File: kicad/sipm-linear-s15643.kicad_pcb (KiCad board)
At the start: 4 copper layers, 113.2 x 74.6 mm, 220 parts, among them J1 SSQ-103-01-G-D, J10 Conn_Coaxial, J11 Conn_Coaxial, J12 Conn_Coaxial, J13 Conn_Coaxial, J14 Conn_Coaxial, J15 Conn_Coaxial, J16 Conn_Coaxial, J17 Conn_Coaxial, J2 Conn_Coaxial, J3 Conn_Coaxial, J4 Conn_Coaxial, J5 Conn_Coaxial, J6 Conn_Coaxial, J7 Conn_Coaxial, J8 Conn_Coaxial, J9 Conn_Coaxial, U1 OPA847IDBVT, U10 OPA847IDBVT, U11 OPA847IDBVT, U12 OPA847IDBVT, U13 OPA847IDBVT, U14 OPA847IDBVT, U15 OPA847IDBVT, U16 OPA847IDBVT, U17 OPA847IDBVT, U2 S15643, U3 OPA847IDBVT, U4 OPA847IDBVT, U5 OPA847IDBVT, U6 OPA847IDBVT, U7 OPA847IDBVT, U8 OPA847IDBVT, U9 OPA847IDBVT

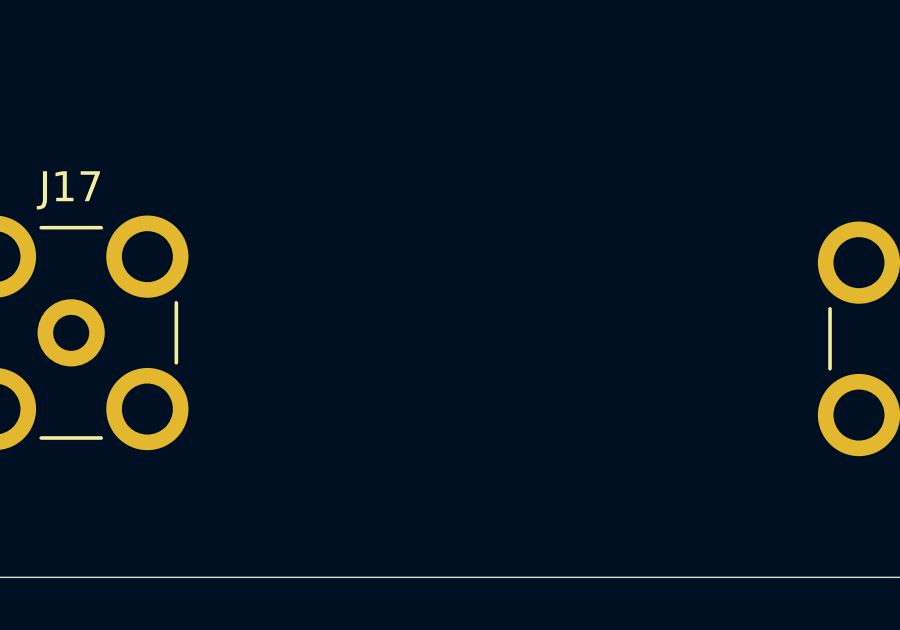
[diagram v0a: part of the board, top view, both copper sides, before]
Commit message: Split power rails across two power supplies
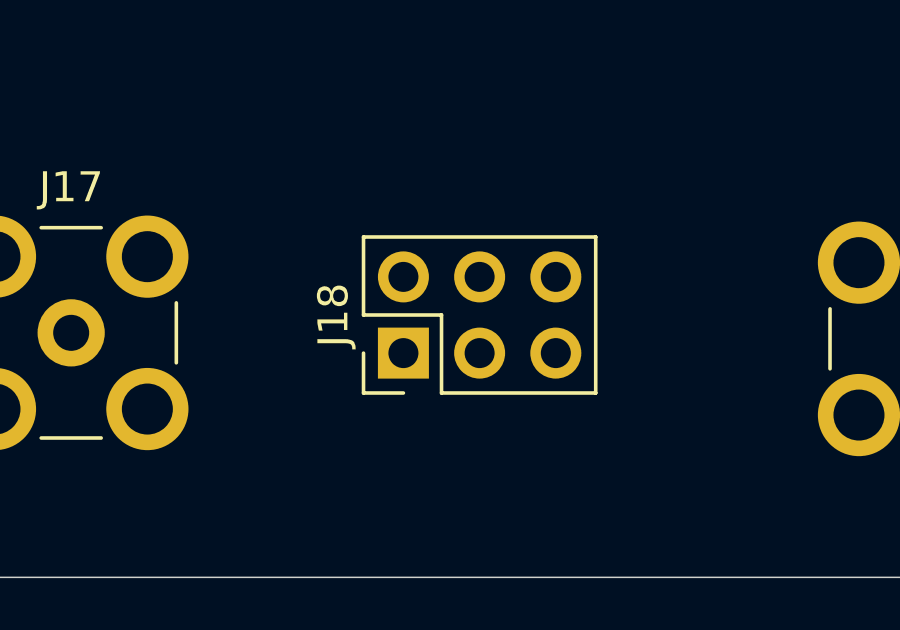
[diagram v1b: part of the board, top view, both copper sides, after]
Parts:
- added J18: SSQ-103-01-G-D, footprints:PinHeader_2x03_P2.54mm_Vertical, F.Cu at (182.7, 135.9)
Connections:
- C31 pad 1: VDDA -> /VSSA2
- C32 pad 1: VSSA -> /VDDA2
- C33 pad 1: VDDA -> /VSSA2
- C34 pad 1: VSSA -> /VDDA2
- C57 pad 1: VDDA -> /VSSA2
- C58 pad 1: VSSA -> /VDDA2
- C59 pad 1: VDDA -> /VSSA2
- C60 pad 1: VSSA -> /VDDA2
- C65 pad 1: VDDA -> /VSSA2
- C66 pad 1: VSSA -> /VDDA2
- C67 pad 1: VDDA -> /VSSA2
- C68 pad 1: VSSA -> /VDDA2
- C73 pad 1: VDDA -> /VSSA2
- C74 pad 1: VSSA -> /VDDA2
- C75 pad 1: VDDA -> /VSSA2
- C76 pad 1: VSSA -> /VDDA2
- J1 pad 1: (no net) -> +5V
- R105 pad 1: /SipmPair7/LINE -> LINE
- R106 pad 2: /SipmPair7/LINE -> LINE
- R14 pad 1: /SipmPair/LINE -> LINE
- R15 pad 2: /SipmPair/LINE -> LINE
- R25 pad 1: /SipmPair2/LINE -> LINE
- R26 pad 2: /SipmPair2/LINE -> LINE
- R37 pad 1: /SipmPair3/LINE -> LINE
- R38 pad 2: /SipmPair3/LINE -> LINE
- R49 pad 1: /SipmPair4/LINE -> LINE
- R50 pad 2: /SipmPair4/LINE -> LINE
- R59 pad 1: (no net) -> /VBias2
- R6 pad 1: /SipmPair1/LINE -> LINE
- R7 pad 2: /SipmPair1/LINE -> LINE
- R81 pad 1: /SipmPair5/LINE -> LINE
- R82 pad 2: /SipmPair5/LINE -> LINE
- R93 pad 1: /SipmPair6/LINE -> LINE
- R94 pad 2: /SipmPair6/LINE -> LINE
- U10 pad 2: VSSA -> /VDDA2
- U10 pad 6: VDDA -> /VSSA2
- U11 pad 2: VSSA -> /VDDA2
- U11 pad 6: VDDA -> /VSSA2
- U14 pad 2: VSSA -> /VDDA2
- U14 pad 6: VDDA -> /VSSA2
- U15 pad 2: VSSA -> /VDDA2
- U15 pad 6: VDDA -> /VSSA2
- U16 pad 2: VSSA -> /VDDA2
- U16 pad 6: VDDA -> /VSSA2
- U17 pad 2: VSSA -> /VDDA2
- U17 pad 6: VDDA -> /VSSA2
- U8 pad 2: VSSA -> /VDDA2
- U8 pad 6: VDDA -> /VSSA2
- U9 pad 2: VSSA -> /VDDA2
- U9 pad 6: VDDA -> /VSSA2
